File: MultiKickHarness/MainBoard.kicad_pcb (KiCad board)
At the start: 2 copper layers, 95.3 x 50.8 mm, 28 parts, among them J1 Mortal Kombat 1 Y-Unit, J2 Mortal Kombat 1 T-Unit, J3 Mortal Kombat 2, J4 Mortal Kombat 3, J5 Ultimate Mortal Kombat 3, J6 Mortal Kombat 4, P0 MOUNTING HOLE, P1 TO CONTROL PANEL

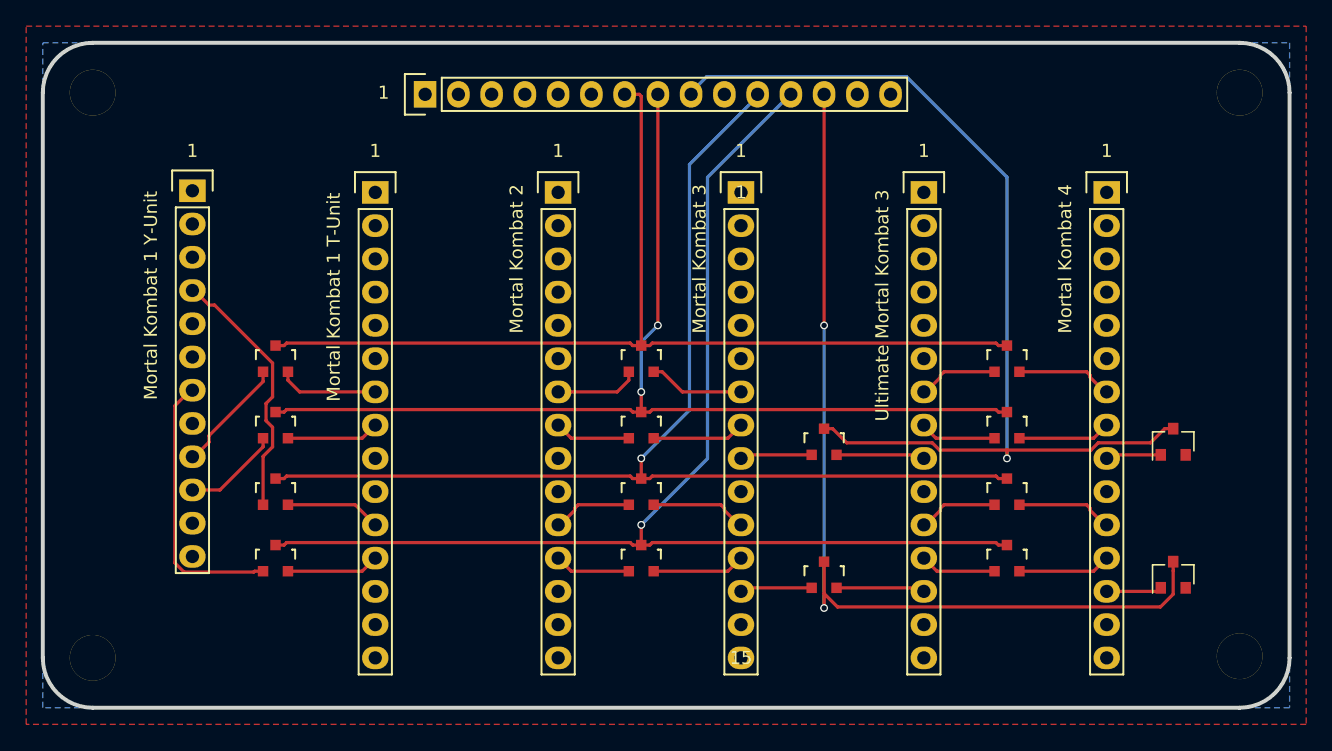
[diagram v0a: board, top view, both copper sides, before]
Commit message: New mount hole positions
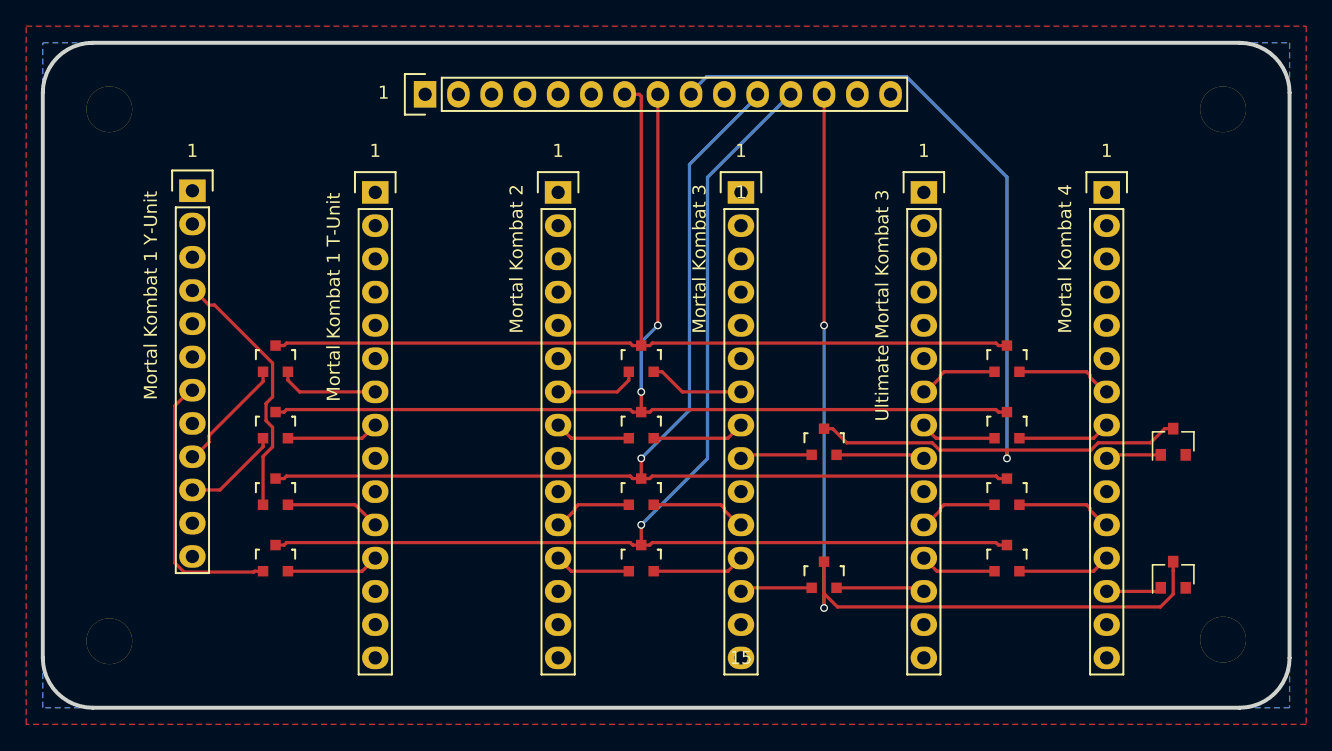
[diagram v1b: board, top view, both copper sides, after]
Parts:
- moved P0 1.80 mm to (168.9, 142.1)
- moved P0 1.80 mm to (168.9, 101.6)
- moved P0 1.80 mm to (83.8, 101.6)
- moved P0 1.80 mm to (83.8, 142.2)
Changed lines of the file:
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@@
     (links 56)
     (no_connects 0)
-    (area 69.6058 94.85412 176.451429 151.287493)
+    (area 78.589999 96.369999 174.140001 147.470001)
     (thickness 1.6)
     (drawings 22)
@@
   )
   (module Mounting_Holes:MountingHole_3-5mm (layer F.Cu)
-    (at 170.18 100.33)
+    (at 168.91 101.6)
     (descr "Mounting hole, Befestigungsbohrung, 3,5mm, No Annular, Kein Restring,")
     (tags "Mounting hole, Befestigungsbohrung, 3,5mm, No Annular, Kein Restring,")
@@
   )
   (module Mounting_Holes:MountingHole_3-5mm (layer F.Cu)
-    (at 170.18 143.383)
+    (at 168.91 142.113)
     (descr "Mounting hole, Befestigungsbohrung, 3,5mm, No Annular, Kein Restring,")
     (tags "Mounting hole, Befestigungsbohrung, 3,5mm, No Annular, Kein Restring,")
@@
   )
   (module Mounting_Holes:MountingHole_3-5mm (layer F.Cu)
-    (at 82.55 143.51)
+    (at 83.82 142.24)
     (descr "Mounting hole, Befestigungsbohrung, 3,5mm, No Annular, Kein Restring,")
     (tags "Mounting hole, Befestigungsbohrung, 3,5mm, No Annular, Kein Restring,")
@@
   )
   (module Mounting_Holes:MountingHole_3-5mm (layer F.Cu)
-    (at 82.55 100.33)
+    (at 83.82 101.6)
     (descr "Mounting hole, Befestigungsbohrung, 3,5mm, No Annular, Kein Restring,")
     (tags "Mounting hole, Befestigungsbohrung, 3,5mm, No Annular, Kein Restring,")
